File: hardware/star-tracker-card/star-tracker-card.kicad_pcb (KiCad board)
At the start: 4 copper layers, 99.8 x 94.6 mm, 329 parts, among them J1 ORESAT-DEBUG-CONNECTOR-CARD, J100 DM3BT-DSF-PEJS, J101 3-1734592-64-1734592-0, J102 FTSH-105-XX-X-DV-K, J3 CONN_03LONGPADS, J4 TFM-120-01-L-D-RA, Q1 MMBT2907, Q2 PMV45EN, Q3 DMP2240UDM, Q4 PMV45EN, Q5 MOSFET-PCH-SOT23-6, Q6 MOSFET-PCH-SOT23-6, U1 RCLAMP0504FB, U10 TLVH431, U11 TCAN330, U12 MIC842LYC5, U13 MIC842LYC5, U14 MAX4211FETE, U15 TPS62112, U16 MAX7310ATE, U17 25AAXX, U18 RCLAMP0504FB, U2 TPS2051CDBVR, U3 THGBMJG7C2LBAU8, U4 SN74LVC1G07DCK, U5 SN74LVC8T245MPWREPPW24-M, U6 CLVCH16T245MDGGREP, U7 OSD3358-512M-BSM, U8 TLV70028QDDCRQ1, U9 TCA9509DGKRDGK8-M, Y1 24MHz, Y2 ABS07-32.768KHZ-T

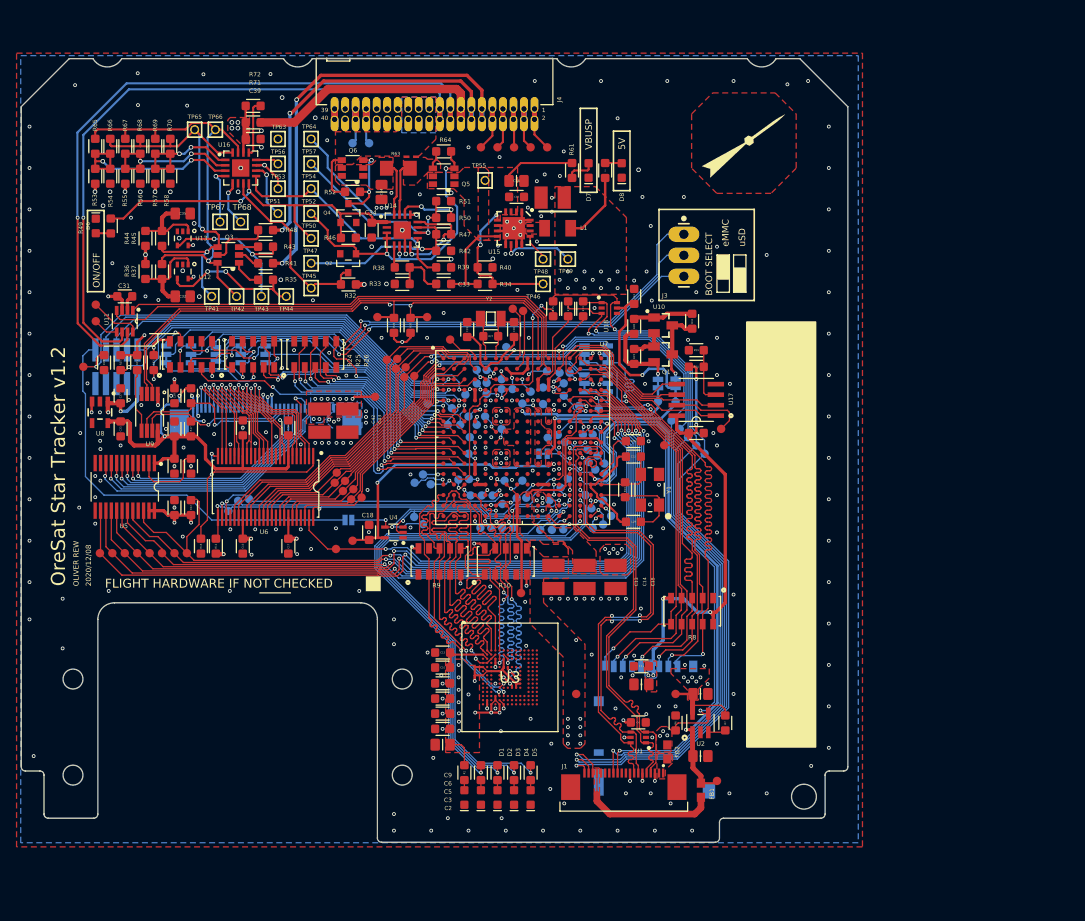
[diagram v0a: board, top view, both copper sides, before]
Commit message: More EAGLE import cleanup
Fixed sheets, did some ERC cleanup, imported into layout, impmorted 4 layer DRC rules.
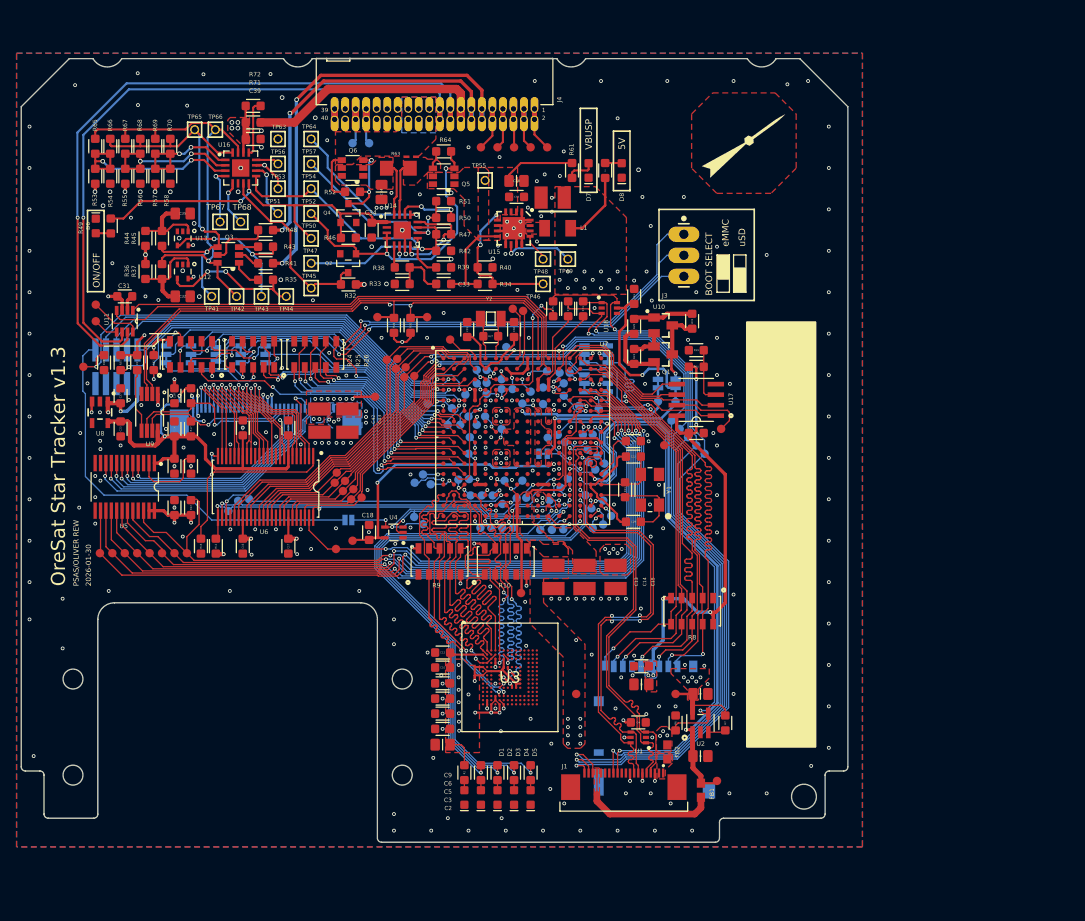
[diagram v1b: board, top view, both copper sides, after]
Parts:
- removed U$1: FLIGHMARKERNEW, star-tracker-card:FLIGHTMARKER_NEW_BOARDS
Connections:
- R35 pad 1: Net-(U12-OUT) -> Net-(R35-Pad1)
- R43 pad 1: Net-(U13-OUT) -> Net-(R43-Pad1)
- TP43 pad 1: Net-(U13-OUT) -> Net-(R43-Pad1)
- TP44 pad 1: Net-(U12-OUT) -> Net-(R35-Pad1)
- U12 pad 4: Net-(U12-OUT) -> unconnected-(U12-OUT-Pad4)
- U13 pad 4: Net-(U13-OUT) -> unconnected-(U13-OUT-Pad4)
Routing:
- net (no net): track 0.00 -> 36.0 mm, vias 0 -> 4
- net Net-(U13-OUT): track 19.0 -> 0.00 mm, vias 2 -> 0
- net Net-(U12-OUT): track 17.0 -> 0.00 mm, vias 2 -> 0
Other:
- board text added: "${ISSUE_DATE}"
- board text added: "OreSat Star Tracker v${REVISION}"
- board text added: "PSAS/OLIVER REW"
- board text removed: "2020/12/08"
- board text removed: "OLIVER REW"
- board text removed: "OreSat Star Tracker v1.2"

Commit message: Daily Push
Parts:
- removed C41: 0.1uF, star-tracker-card:.0603-A
- removed C44, C7: 10uF, star-tracker-card:.0805-B
- removed FB1: 30Ω/1.8A, star-tracker-card:0603
- removed J102: FTSH-105-XX-X-DV-K, star-tracker-card:CON10_2X5_DUK_FTSH
- removed JP1: JUMPER-SMT_2_NO_SILK, star-tracker-card:SMT-JUMPER_2_NO_SILK
- removed JP100: JUMPER-SMT_2_NC_TRACE_SILK, star-tracker-card:SMT-JUMPER_2_NC_TRACE_SILK
- removed R74, R75: 100, star-tracker-card:.0603-A
- removed TP112, TP151, TP155, TP58, TP59: TEST-POINT3X4, star-tracker-card:PAD.03X.04
- removed U18: RCLAMP0504FB, star-tracker-card:SC70-6
- added C45: 10u 25V 0805, Capacitor_SMD:C_1206_3216Metric, F.Cu at (222.8, 66.8)
- added C46: 470n, oresat-passives:c_0603-SMALL, F.Cu at (221.7, 73.8)
- added R76: 10k, oresat-passives:0603-C-NOSILK, F.Cu at (221.6, 75.9)
- added TP32: Test-Point, oresat-misc:TestPoint_Pad_D1.0mm, F.Cu at (221.1, 69.6)
- added TP71: TEST-POINT3X4, oresat-misc:TestPoint_Pad_D1.0mm, F.Cu at (216.8, 66.2)
- added TP72: TEST-POINT3X4, oresat-misc:TestPoint_Pad_D1.0mm, F.Cu at (216.8, 68.6)
- added TP73: TEST-POINT3X4, oresat-misc:TestPoint_Pad_D1.0mm, F.Cu at (216.8, 70.9)
- added TP74: TEST-POINT3X4, oresat-misc:TestPoint_Pad_D1.0mm, F.Cu at (212.5, 66.2)
- added TP75: TEST-POINT3X4, oresat-misc:TestPoint_Pad_D1.0mm, F.Cu at (212.5, 68.6)
- added TP76: TEST-POINT3X4, oresat-misc:TestPoint_Pad_D1.0mm, F.Cu at (212.5, 70.9)
- added TP77: TEST-POINT3X4, oresat-misc:TestPoint_Pad_D1.0mm, F.Cu at (212.5, 73.2)
- C1: value 10uF -> 100n; footprint star-tracker-card:.0805-B -> oresat-passives:c_0603-SMALL
- C10, C11, C12, C16, C17, C18, C19, C20, C21, C22, C23, C24, C25, C26, C27, C28, C29, C3, C30, C31, C33, C34, C37, C39, C4, C40, C5, C6, C9: footprint star-tracker-card:.0603-A -> oresat-passives:c_0603-SMALL
- C13, C14, C15, C36, C42, C43: footprint star-tracker-card:C1210 -> oresat-passives:0805-B-NOSILK
- C2, C38, C8: footprint star-tracker-card:.0805-B -> oresat-passives:0805-B-NOSILK
- C32, C35: footprint star-tracker-card:.0805-B-NOSILK -> oresat-passives:0805-C-NOSILK
- J1: footprint star-tracker-card:TE_2-1734592-0 -> oresat-connectors:J-JST-SM14BSHLSTF
- J4: footprint star-tracker-card:J-SAMTEC-TFM-120-X1-XXX-D-RA -> oresat-connectors:J-SAMTEC-TFM-120-X1-XXX-D-RA
- L1: footprint star-tracker-card:ECS-MPI4040 -> oresat-passives:L_ECS-MPI4040
- Q5, Q6: value MOSFET-PCH-SOT23-6 -> DMP3050LVT-7; footprint star-tracker-card:SOT23-6 -> Package_TO_SOT_SMD:TSOT-23-6
- R1, R11, R12, R13, R14, R15, R16, R17, R18, R19, R2, R20, R21, R22, R23, R27, R28, R29, R3, R30, R31, R32, R33, R34, R35, R36, R37, R38, R39, R4, R40, R41, R42, R43, R44, R45, R46, R47, R48, R49, R5, R50, R51, R52, R53, R54, R55, R56, R57, R58, R59, R6, R60, R61, R62, R64, R65, R66, R67, R68, R69, R70, R71, R72, R73: footprint star-tracker-card:.0603-A -> Resistor_SMD:R_0603_1608Metric
- R63: footprint star-tracker-card:R1206_334 -> Resistor_SMD:R_1206_3216Metric
- R7: value 10k -> 100; footprint star-tracker-card:.0603-A -> Resistor_SMD:R_0603_1608Metric
- TP1, TP10, TP100, TP101, TP102, TP103, TP104, TP105, TP106, TP107, TP108, TP109, TP11, TP110, TP111, TP113, TP114, TP115, TP116, TP117, TP118, TP119, TP12, TP120, TP121, TP122, TP123, TP124, TP125, TP126, TP127, TP128, TP129, TP13, TP130, TP131, TP132, TP133, TP134, TP135, TP136, TP137, TP138, TP139, TP14, TP140, TP141, TP142, TP143, TP144, TP145, TP146, TP147, TP148, TP149, TP15, TP150, TP152, TP153, TP154, TP156, TP157, TP158, TP159, TP16, TP160, TP161, TP162, TP163, TP164, TP165, TP166, TP167, TP168, TP169, TP17, TP170, TP171, TP172, TP173, TP174, TP175, TP176, TP177, TP178, TP179, TP18, TP180, TP181, TP182, TP183, TP184, TP19, TP2, TP20, TP21, TP22, TP23, TP24, TP25, TP26, TP27, TP28, TP29, TP3, TP30, TP31, TP35, TP36, TP37, TP38, TP39, TP4, TP40, TP5, TP6, TP60, TP61, TP62, TP69, TP7, TP8, TP9: footprint star-tracker-card:PAD.03X.04 -> oresat-misc:TestPoint_Pad_D1.0mm
- TP63: footprint star-tracker-card:2MM-TEST-POINT -> star-tracker-card:PAD.03X.04
- U12, U13: footprint star-tracker-card:SC70-5 -> Package_TO_SOT_SMD:SOT-353_SC-70-5
- U14, U16: footprint star-tracker-card:QFN65P400X400X80-17T210 -> Package_DFN_QFN:QFN-16-1EP_4x4mm_P0.65mm_EP2.1x2.1mm
- U15: footprint star-tracker-card:S-PVQFN-16 -> Package_DFN_QFN:Texas_RSA_VQFN-16-1EP_4x4mm_P0.65mm_EP2.7x2.7mm
- U2: value TPS2051CDBVR -> TS5A21366DCUR; footprint star-tracker-card:DBV5 -> Package_SO:VSSOP-8_2.3x2mm_P0.5mm
- U4: footprint star-tracker-card:C70(TI-DCK) -> Package_TO_SOT_SMD:SOT-353_SC-70-5
- moved TP65 13.6 mm to (107.1, 71.8)
- moved J1 12.3 mm to (174.9, 157.4), turned to 0 degrees
- moved TP66 11.7 mm to (111.8, 71.8)
- moved R54 9.26 mm to (104.5, 64.0), turned to 180 degrees
- moved R7 8.35 mm to (189.8, 143.6)
- moved R56 8.25 mm to (110.5, 64.0), turned to 180 degrees
- moved R58 7.86 mm to (116.5, 64.0), turned to 180 degrees
- moved R53 7.06 mm to (104.5, 65.5), turned to 180 degrees
- moved R57 6.57 mm to (116.5, 65.5), turned to 0 degrees
- moved R55 6.39 mm to (110.5, 65.5), turned to 0 degrees
- moved R69 6.29 mm to (119.5, 64.0), turned to 0 degrees
- moved R6 5.28 mm to (181.7, 141.3), turned to 180 degrees
- moved C1 5.27 mm to (177.7, 137.5), turned to -90 degrees
- moved R67 4.81 mm to (113.5, 64.0), turned to 180 degrees
- moved R65 4.23 mm to (107.5, 64.0), turned to 180 degrees
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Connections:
- net /star-tracker-card_2/BOOT0 renamed /Card Power Domain/BOOT0
- net /star-tracker-card_2/CB-RESET renamed /Card Power Domain/CB-RESET
- net /star-tracker-card_2/CB_CTRL renamed /Card Power Domain/CB_CTRL
- net /star-tracker-card_2/PB6/SCL renamed /Card Power Domain/PB6/SCL
- net /star-tracker-card_2/PB7/SDA renamed /Card Power Domain/PB7/SDA
- net /star-tracker-card_2/POUT renamed /Card Power Domain/POUT
- net /star-tracker-card_2/~{FAULT} renamed /Card Power Domain/~{FAULT}
- net /star-tracker-card_3/CLK_EN_E renamed /CLK_EN_E
- net /star-tracker-card_3/D0_E renamed /D0_E
- net /star-tracker-card_3/D10_E renamed /D10_E
- net /star-tracker-card_3/D11_E renamed /D11_E
- net /star-tracker-card_3/D1_E renamed /D1_E
- net /star-tracker-card_3/D2_E renamed /D2_E
- net /star-tracker-card_3/D3_E renamed /D3_E
- net /star-tracker-card_3/D4_E renamed /D4_E
- net /star-tracker-card_3/D5_E renamed /D5_E
- net /star-tracker-card_3/D6_E renamed /D6_E
- net /star-tracker-card_3/D7_E renamed /D7_E
- net /star-tracker-card_3/D8_E renamed /D8_E
- net /star-tracker-card_3/D9_E renamed /D9_E
- net /star-tracker-card_3/FLASH_E renamed /FLASH_E
- net /star-tracker-card_3/HSYNC_E renamed /HSYNC_E
- net /star-tracker-card_3/I2C2_SCL renamed /I2C2_SCL
- net /star-tracker-card_3/I2C2_SDA renamed /I2C2_SDA
- net /star-tracker-card_3/PIXCLK_E renamed /PIXCLK_E
- net /star-tracker-card_3/SADDR_E renamed /SADDR_E
- net /star-tracker-card_3/STANDBY_E renamed /STANDBY_E
- net /star-tracker-card_3/TRIGGER_E renamed /TRIGGER_E
- net /star-tracker-card_3/VREG_EN_E renamed /VREG_EN_E
- net /star-tracker-card_3/VSYNC_E renamed /VSYNC_E
- net /star-tracker-card_3/~{OE_E} renamed /~{OE_E}
- net /star-tracker-card_3/~{RESET_E} renamed /~{RESET_E}
- net /star-tracker-card_4/OSC0_GND renamed /SIP B/OSC0_GND
- net /star-tracker-card_4/OSC0_IN renamed /SIP B/OSC0_IN
- net /star-tracker-card_4/OSC0_OUT renamed /SIP B/OSC0_OUT
- net CAN2_H renamed /CAN2_H
- net CAN2_L renamed /CAN2_L
- net OPD_PWR renamed /OPD_PWR
- net OPD_SCL renamed /OPD_SCL
- net OPD_SDA renamed /OPD_SDA
- net USB_CLI_VBUS renamed /V_USB
- C1 pad 1: /star-tracker-card_4/VOUT_USB -> /Card Power Domain/ON/~{OFF}
- C13 pad 1: VIN_USB -> /SIP A, E ,F/VIN_USB
- C34 pad 1: /star-tracker-card_2/ON/~{OFF} -> /Card Power Domain/ON/~{OFF}
- C4 pad 1: VIN_USB -> /SIP A, E ,F/VIN_USB
- D1 pad A: Net-(D1-PadA) -> (no net)
- D1 pad C: GND -> (no net)
- D2 pad A: Net-(D2-PadA) -> (no net)
- D2 pad C: GND -> (no net)
- D3 pad A: Net-(D3-PadA) -> (no net)
- D3 pad C: GND -> (no net)
- D4 pad A: Net-(D4-PadA) -> (no net)
- D4 pad C: GND -> (no net)
- D5 pad A: Net-(D5-PadA) -> (no net)
- D5 pad C: GND -> (no net)
- D6 pad A: Net-(D6-PadA) -> (no net)
- D6 pad C: GND -> (no net)
- D7 pad A: Net-(D7-PadA) -> (no net)
- D7 pad C: GND -> (no net)
- D8 pad A: Net-(D8-PadA) -> (no net)
- D8 pad C: GND -> (no net)
- FB2 pad 2: VIN_USB -> /SIP A, E ,F/VIN_USB
- J1 pad 12: UART0_RX -> unconnected-(J1-SWCLK-Pad12)
- J1 pad 13: UART0_TX -> unconnected-(J1-SWO-Pad13)
- J1 pad 14: unconnected-(J1-SWDIO-Pad14) -> GND
- J1 pad 15: unconnected-(J1-SWCLK-Pad15) -> GND
- J1 pad 16: unconnected-(J1-SWO-Pad16) -> GND
- J1 pad 3: GND -> /USB_CLI_P
- J1 pad 4: USB_CLI_P -> /USB_CLI_N
- J1 pad 5: USB_CLI_N -> GND
- J1 pad 6: GND -> /UART0_TX
- J1 pad 7: USB_HO_PX -> /UART0_RX
- J1 pad 8: USB_HO_N -> Net-(J1-DEBUG-0)
- J1 pad 9: GND -> unconnected-(J1-VTARGET-Pad9)
- J4 pad 1: /star-tracker-card_1/N$103 -> Net-(J4-Pad1)
- J4 pad 10: /star-tracker-card_1/SPARE1 -> unconnected-(J4-Pad10)
- J4 pad 2: /star-tracker-card_1/N$103 -> Net-(J4-Pad1)
- J4 pad 21: VBUS -> unconnected-(J4-Pad21)
- J4 pad 22: VBUS -> unconnected-(J4-Pad22)
- J4 pad 3: /star-tracker-card_1/SPARE4 -> Net-(J4-Pad3)
- J4 pad 31: GND -> unconnected-(J4-Pad31)
- J4 pad 32: GND -> Net-(J4-Pad32)
- J4 pad 33: /star-tracker-card_1/CAN1_H -> Net-(J4-Pad32)
- J4 pad 34: /star-tracker-card_1/CAN1_H -> Net-(J4-Pad34)
- J4 pad 35: /star-tracker-card_1/CAN1_L -> Net-(J4-Pad34)
- J4 pad 36: /star-tracker-card_1/CAN1_L -> unconnected-(J4-Pad36)
- J4 pad 37: GND -> /C3-UART-TX
- J4 pad 38: GND -> /C3-UART-RX
- J4 pad 39: /star-tracker-card_1/~{SD} -> unconnected-(J4-Pad39)
- J4 pad 4: /star-tracker-card_1/SPARE4 -> Net-(J4-Pad3)
- J4 pad 40: /star-tracker-card_1/~{SD} -> unconnected-(J4-Pad40)
- J4 pad 5: /star-tracker-card_1/SPARE3 -> Net-(J4-Pad5)
- J4 pad 6: /star-tracker-card_1/SPARE3 -> Net-(J4-Pad5)
- J4 pad 7: /star-tracker-card_1/SPARE2 -> unconnected-(J4-Pad7)
- J4 pad 8: /star-tracker-card_1/SPARE2 -> unconnected-(J4-Pad8)
- J4 pad 9: /star-tracker-card_1/SPARE1 -> unconnected-(J4-Pad9)
- JP101 pad 1: Net-(TP165-1) -> Net-(U7A-SYS_VDD3_3P3V@1)
- JP102 pad 1: /star-tracker-card_3/D0_I -> /Camera Logical Level Shifters/D0_I
- JP103 pad 1: /star-tracker-card_3/D1_I -> /Camera Logical Level Shifters/D1_I
- JP110 pad 1: /star-tracker-card_3/D2_I -> /Camera Logical Level Shifters/D2_I
- JP111 pad 1: /star-tracker-card_3/D3_I -> /SIP C/D3_I
- Q3 pad 2: Net-(Q3B-S) -> /Card Power Domain/PEN-SDA-FILT
- Q3 pad 4: /star-tracker-card_2/PEN-SDA-FILT -> Net-(Q3B-D)
- Q3 pad 5: Net-(Q3A-S) -> /Card Power Domain/PEN-SCL-FILT
- Q3 pad 6: /star-tracker-card_2/PEN-SCL-FILT -> Net-(Q3A-D)
- Q4 pad 1: /star-tracker-card_2/ON/~{OFF} -> /Card Power Domain/ON/~{OFF}
- Q5 pad 1: VBUSP -> Net-(U14-RS-)
- Q5 pad 2: VBUSP -> Net-(U14-RS-)
- Q5 pad 4: Net-(Q5-S) -> VBUSP
- Q5 pad 5: VBUSP -> Net-(U14-RS-)
- Q5 pad 6: VBUSP -> Net-(U14-RS-)
- Q6 pad 1: Net-(U14-RS+) -> VBUS
- Q6 pad 2: Net-(U14-RS+) -> VBUS
- Q6 pad 4: VBUS -> Net-(Q6-S)
- Q6 pad 5: Net-(U14-RS+) -> VBUS
- Q6 pad 6: Net-(U14-RS+) -> VBUS
- R1 pad 2: Net-(D1-PadA) -> Net-(D1-A)
- R11 pad 1: /star-tracker-card_3/BUS_OE -> /Camera Logical Level Shifters/BUS_OE
- R12 pad 1: /star-tracker-card_3/INPUT_EN -> /Camera Logical Level Shifters/INPUT_EN
- R19 pad 2: Net-(TP31-1) -> Net-(U7B-TRSTN)
- R2 pad 2: Net-(D2-PadA) -> Net-(D2-A)
- R29 pad 2: /star-tracker-card_3/SDA_2 -> /Camera Logical Level Shifters/SDA_2
- R3 pad 2: Net-(D3-PadA) -> Net-(D3-A)
- R30 pad 2: /star-tracker-card_3/SCL_2 -> /Camera Logical Level Shifters/SCL_2
- R35 pad 1: Net-(R35-Pad1) -> Net-(U12-OUT)
- R37 pad 2: /star-tracker-card_2/PEN-SCL-FILT -> /Card Power Domain/PEN-SCL-FILT
- R4 pad 2: Net-(D4-PadA) -> Net-(D4-A)
- R41 pad 2: Net-(Q3B-S) -> Net-(Q3B-D)
- R43 pad 1: Net-(R43-Pad1) -> Net-(U13-OUT)
- R45 pad 2: /star-tracker-card_2/PEN-SDA-FILT -> /Card Power Domain/PEN-SDA-FILT
- R46 pad 2: /star-tracker-card_2/ON/~{OFF} -> /Card Power Domain/ON/~{OFF}
- R48 pad 2: Net-(Q3A-S) -> Net-(Q3A-D)
- R49 pad 1: Net-(D6-PadA) -> Net-(D6-A)
- R49 pad 2: /star-tracker-card_2/ON/~{OFF} -> /Card Power Domain/ON/~{OFF}
- R5 pad 2: Net-(D5-PadA) -> Net-(D5-A)
- R53 pad 1: /star-tracker-card_2/AD2 -> /Card Power Domain/AD2
- R54 pad 1: GND -> /Card Power Domain/AD2
- R54 pad 2: /star-tracker-card_2/AD2 -> GND
- R55 pad 1: /star-tracker-card_2/AD1 -> VPD
- R55 pad 2: VPD -> /Card Power Domain/AD1
- R56 pad 1: GND -> /Card Power Domain/AD1
- R56 pad 2: /star-tracker-card_2/AD1 -> GND
- R57 pad 1: /star-tracker-card_2/AD0 -> VPD
- R57 pad 2: VPD -> /Card Power Domain/AD0
- R58 pad 1: GND -> /Card Power Domain/AD0
- R58 pad 2: /star-tracker-card_2/AD0 -> GND
- R6 pad 2: Net-(U2-EN) -> Net-(U16-IO7)
- R61 pad 1: Net-(D7-PadA) -> Net-(D7-A)
- R62 pad 1: Net-(D8-PadA) -> Net-(D8-A)
- R63 pad 1: Net-(U14-RS+) -> Net-(Q6-S)
- R63 pad 2: Net-(Q5-S) -> Net-(U14-RS-)
- R64 pad 2: Net-(Q5-S) -> Net-(U14-RS-)
- R65 pad 1: /star-tracker-card_2/PEN-SCL-FILT -> /Card Power Domain/PEN-SCL-FILT
- R65 pad 2: /star-tracker-card_2/AD2 -> /Card Power Domain/AD2
- R66 pad 1: /star-tracker-card_2/AD2 -> /Card Power Domain/PEN-SDA-FILT
- R66 pad 2: /star-tracker-card_2/PEN-SDA-FILT -> /Card Power Domain/AD2
- R67 pad 1: /star-tracker-card_2/PEN-SCL-FILT -> /Card Power Domain/PEN-SCL-FILT
- R67 pad 2: /star-tracker-card_2/AD1 -> /Card Power Domain/AD1
- R68 pad 1: /star-tracker-card_2/AD1 -> /Card Power Domain/PEN-SDA-FILT
- R68 pad 2: /star-tracker-card_2/PEN-SDA-FILT -> /Card Power Domain/AD1
- R69 pad 1: /star-tracker-card_2/PEN-SCL-FILT -> /Card Power Domain/AD0
- R69 pad 2: /star-tracker-card_2/AD0 -> /Card Power Domain/PEN-SCL-FILT
- R7 pad 1: Net-(U2-~{FLT}) -> /C3-UART-RX
- R7 pad 2: VDD -> Net-(U2-NO1)
- R70 pad 1: /star-tracker-card_2/AD0 -> /Card Power Domain/PEN-SDA-FILT
- R70 pad 2: /star-tracker-card_2/PEN-SDA-FILT -> /Card Power Domain/AD0
- R73 pad 1: I2C0_SCL -> /C3-UART-TX
- R73 pad 2: Net-(U7A-I2C0_SCL) -> Net-(U2-NO2)
- TP41 pad 1: /star-tracker-card_2/PEN-SDA-FILT -> /Card Power Domain/PEN-SDA-FILT
- TP42 pad 1: /star-tracker-card_2/PEN-SCL-FILT -> /Card Power Domain/PEN-SCL-FILT
- TP43 pad 1: Net-(R43-Pad1) -> Net-(U13-OUT)
- TP44 pad 1: Net-(R35-Pad1) -> Net-(U12-OUT)
- TP50 pad 1: /star-tracker-card_2/ON/~{OFF} -> /Card Power Domain/ON/~{OFF}
- TP65 pad 1: /star-tracker-card_2/PEN-SDA-FILT -> /Card Power Domain/PEN-SDA-FILT
- TP66 pad 1: /star-tracker-card_2/PEN-SCL-FILT -> /Card Power Domain/PEN-SCL-FILT
- U1 pad 1: USB_CLI_N -> /USB_CLI_N
- U1 pad 3: USB_CLI_P -> /USB_CLI_P
- U1 pad 4: USB_HO_PX -> unconnected-(U1-I3-Pad4)
- U1 pad 5: VIN_USB -> /SIP A, E ,F/VIN_USB
- U1 pad 6: USB_HO_N -> unconnected-(U1-I4-Pad6)
- U11 pad 5: Net-(TP35-1) -> Net-(U11-SHDN)
- U11 pad 8: Net-(TP40-1) -> Net-(U11-S)
- U12 pad 3: (no net) -> unconnected-(U12-Pad3)
- U12 pad 4: unconnected-(U12-OUT-Pad4) -> Net-(U12-OUT)
- U13 pad 3: (no net) -> unconnected-(U13-Pad3)
- U13 pad 4: unconnected-(U13-OUT-Pad4) -> Net-(U13-OUT)
- U14 pad 1: /star-tracker-card_2/ON/~{OFF} -> /Card Power Domain/ON/~{OFF}
- U14 pad 15: Net-(Q5-S) -> Net-(U14-RS-)
- U14 pad 16: Net-(U14-RS+) -> Net-(Q6-S)
- U14 pad 2: (no net) -> /Card Power Domain/ON/~{OFF}
- U16 pad 1: /star-tracker-card_2/AD0 -> /Card Power Domain/AD0
- U16 pad 15: /star-tracker-card_2/PEN-SCL-FILT -> /Card Power Domain/PEN-SCL-FILT
- U16 pad 16: /star-tracker-card_2/PEN-SDA-FILT -> /Card Power Domain/PEN-SDA-FILT
- U16 pad 2: /star-tracker-card_2/AD1 -> /Card Power Domain/AD1
- U16 pad 3: /star-tracker-card_2/AD2 -> /Card Power Domain/AD2
- U16 pad 8: /star-tracker-card_2/ON/~{OFF} -> /Card Power Domain/ON/~{OFF}
- U17 pad 7: Net-(TP69-1) -> Net-(U17-~{HOLD})
- U2 pad 1: /star-tracker-card_4/VOUT_USB -> Net-(U2-NO1)
- U2 pad 2: GND -> /UART0_TX
- U2 pad 3: Net-(U2-~{FLT}) -> Net-(U16-IO7)
- U2 pad 4: Net-(U2-EN) -> GND
- U2 pad 5: VDD -> Net-(U2-NO2)
- U4 pad 1: (no net) -> unconnected-(U4-Pad1)
- U4 pad 2: /star-tracker-card_5/PMIC_PGOOD -> /SIP A, E ,F/PMIC_PGOOD
- U4 pad 4: RESET# -> Net-(U4-Y)
- U5 pad 14: /star-tracker-card_3/VREG_EN -> /Camera Logical Level Shifters/VREG_EN
- U5 pad 15: /star-tracker-card_3/TRIGGER -> /Camera Logical Level Shifters/TRIGGER
- U5 pad 16: /star-tracker-card_3/SADDR -> /Camera Logical Level Shifters/SADDR
- U5 pad 17: /star-tracker-card_3/CAM_OE -> /Camera Logical Level Shifters/CAM_OE
- U5 pad 18: /star-tracker-card_3/STANDBY -> /Camera Logical Level Shifters/STANDBY
- U5 pad 19: /star-tracker-card_3/RESET -> /Camera Logical Level Shifters/RESET
- U5 pad 20: /star-tracker-card_3/CLK_EN -> /Camera Logical Level Shifters/CLK_EN
- U5 pad 22: /star-tracker-card_3/INPUT_EN -> /Camera Logical Level Shifters/INPUT_EN
- U6 pad 25: /star-tracker-card_3/BUS_OE -> /Camera Logical Level Shifters/BUS_OE
- U6 pad 26: /star-tracker-card_3/VSYNC_I -> /Camera Logical Level Shifters/VSYNCI
- U6 pad 27: /star-tracker-card_3/HSYNC_I -> /Camera Logical Level Shifters/HSYNC_I
- U6 pad 29: /star-tracker-card_3/PIXCLK_I -> /Camera Logical Level Shifters/PIXCLK_I
- U6 pad 30: /star-tracker-card_3/D6_I -> /Camera Logical Level Shifters/D6_I
- U6 pad 32: /star-tracker-card_3/D5_I -> /Camera Logical Level Shifters/D5_I
- U6 pad 33: /star-tracker-card_3/D4_I -> /Camera Logical Level Shifters/D4_I
- U6 pad 35: /star-tracker-card_3/D3_I -> /SIP C/D3_I
- U6 pad 36: /star-tracker-card_3/D2_I -> /Camera Logical Level Shifters/D2_I
- U6 pad 37: /star-tracker-card_3/D1_I -> /Camera Logical Level Shifters/D1_I
- U6 pad 38: /star-tracker-card_3/D0_I -> /Camera Logical Level Shifters/D0_I
- U6 pad 40: /star-tracker-card_3/D7_I -> /Camera Logical Level Shifters/D7_I
- U6 pad 41: /star-tracker-card_3/D8_I -> /Camera Logical Level Shifters/D8_I
- U6 pad 43: /star-tracker-card_3/D9_I -> /Camera Logical Level Shifters/D9_I
- U6 pad 44: /star-tracker-card_3/D10_I -> /Camera Logical Level Shifters/D10_I
- U6 pad 46: /star-tracker-card_3/D11_I -> /Camera Logical Level Shifters/D11_I
- U6 pad 47: /star-tracker-card_3/FLASH -> /Camera Logical Level Shifters/FLASH
- U6 pad 48: /star-tracker-card_3/BUS_OE -> /Camera Logical Level Shifters/BUS_OE
- U7 pad A1: /star-tracker-card_3/D4_I -> /Camera Logical Level Shifters/D4_I
- U7 pad A10: /star-tracker-card_3/SCL_2 -> /Camera Logical Level Shifters/SCL_2
- U7 pad A12: UART0_RX -> /UART0_RX
- U7 pad A2: /star-tracker-card_3/D5_I -> /Camera Logical Level Shifters/D5_I
- U7 pad A3: /star-tracker-card_3/D8_I -> /Camera Logical Level Shifters/D8_I
- U7 pad A4: Net-(TP30-1) -> Net-(U7C-XDMA_EVENT_INTR0)
- U7 pad A7: Net-(TP182-1) -> Net-(U7B-SYS_ADC_1P8V)
- U7 pad A8: Net-(TP39-1) -> Net-(U7B-AIN0)
- U7 pad A9: Net-(TP171-1) -> Net-(U7B-AGND_ADC)
- U7 pad B1: /star-tracker-card_3/D7_I -> /Camera Logical Level Shifters/D7_I
- U7 pad B10: /star-tracker-card_3/SDA_2 -> /Camera Logical Level Shifters/SDA_2
- U7 pad B12: UART0_TX -> /UART0_TX
- U7 pad B2: /star-tracker-card_3/D6_I -> /Camera Logical Level Shifters/D6_I
- U7 pad B3: /star-tracker-card_3/D9_I -> /Camera Logical Level Shifters/D9_I
- U7 pad B4: /star-tracker-card_3/PIXCLK_I -> /Camera Logical Level Shifters/PIXCLK_I
- U7 pad B6: Net-(TP181-1) -> Net-(U7B-AIN2)
- U7 pad B7: Net-(TP171-1) -> Net-(U7B-AGND_ADC)
- U7 pad B8: Net-(TP38-1) -> Net-(U7B-AIN1)
- U7 pad B9: Net-(TP171-1) -> Net-(U7B-AGND_ADC)
- U7 pad C1: Net-(J102-NC/TDI) -> unconnected-(U7B-TDI-PadC1)
- U7 pad C12: Net-(TP177-1) -> Net-(U7C-UART0_CTSN)
- U7 pad C13: Net-(TP178-1) -> Net-(U7C-UART0_RTSN)
- U7 pad C2: Net-(J102-SWO/TDO) -> unconnected-(U7B-TDO-PadC2)
- U7 pad C3: /star-tracker-card_3/D10_I -> /Camera Logical Level Shifters/D10_I
- U7 pad C4: /star-tracker-card_3/D11_I -> /Camera Logical Level Shifters/D11_I
- U7 pad C5: Net-(TP180-1) -> Net-(U7C-ECAP0_IN_PWM0_OUT)
- U7 pad C6: Net-(TP175-1) -> Net-(U7B-AIN3)
- U7 pad C7: Net-(TP176-1) -> Net-(U7B-AIN4)
- U7 pad C8: Net-(TP169-1) -> Net-(U7B-AIN5)
- U7 pad C9: Net-(TP179-1) -> Net-(U7B-AIN6)
- U7 pad D1: Net-(J102-SWDCLK/TCK) -> unconnected-(U7B-TCK-PadD1)
- U7 pad D12: Net-(TP172-1) -> Net-(U7F-NC@1)
- U7 pad D13: Net-(TP174-1) -> Net-(U7D-MDC)
- U7 pad D14: /star-tracker-card_3/STANDBY -> /Camera Logical Level Shifters/STANDBY
- U7 pad D15: /star-tracker-card_3/SADDR -> /Camera Logical Level Shifters/SADDR
- U7 pad D16: /star-tracker-card_3/RESET -> /Camera Logical Level Shifters/RESET
- U7 pad D2: Net-(J102-SWDIO/TMS) -> unconnected-(U7B-TMS-PadD2)
- U7 pad D3: Net-(TP31-1) -> Net-(U7B-TRSTN)
- U7 pad D4: Net-(TP167-1) -> Net-(U7A-EXTINTN)
- U7 pad D5: Net-(TP173-1) -> Net-(U7F-CAP_VDD_RTC)
- U7 pad D6: Net-(TP168-1) -> Net-(U7B-PMIC_MUX_OUT)
- U7 pad D7: Net-(TP170-1) -> Net-(U7B-AIN7)
- U7 pad E1: Net-(TP159-1) -> Net-(U7D-LCD_AC_BIAS_EN)
- U7 pad E13: Net-(TP158-1) -> Net-(U7D-MDIO)
- U7 pad E14: /star-tracker-card_3/INPUT_EN -> /Camera Logical Level Shifters/INPUT_EN
- U7 pad E15: /star-tracker-card_3/TRIGGER -> /Camera Logical Level Shifters/TRIGGER
- U7 pad E16: /star-tracker-card_3/CLK_EN -> /Camera Logical Level Shifters/CLK_EN
- U7 pad E4: Net-(TP167-1) -> Net-(U7A-EXTINTN)
- U7 pad F1: Net-(TP162-1) -> Net-(U7D-LCD_PCLK)
- U7 pad F10: Net-(TP163-1) -> Net-(U7A-SYS_VDD_1P8V@1)
- U7 pad F11: Net-(TP161-1) -> Net-(U7A-SYS_VDD2_3P3V@1)
- U7 pad F13: Net-(TP160-1) -> Net-(U7F-VDD_MPU)
- U7 pad F14: /star-tracker-card_3/BUS_OE -> /Camera Logical Level Shifters/BUS_OE
- U7 pad F15: /star-tracker-card_3/CAM_OE -> /Camera Logical Level Shifters/CAM_OE
- U7 pad F16: /star-tracker-card_3/VREG_EN -> /Camera Logical Level Shifters/VREG_EN
- U7 pad F2: Net-(TP152-1) -> Net-(U7D-LCD_HSYNC)
- U7 pad F3: Net-(TP153-1) -> Net-(U7D-LCD_VSYNC)
- U7 pad F4: Net-(TP156-1) -> Net-(U7F-VDDS_DDR)
- U7 pad F8: Net-(TP165-1) -> Net-(U7A-SYS_VDD3_3P3V@1)
- U7 pad F9: Net-(TP165-1) -> Net-(U7A-SYS_VDD3_3P3V@1)
- U7 pad G10: Net-(TP163-1) -> Net-(U7A-SYS_VDD_1P8V@1)
- U7 pad G11: Net-(TP161-1) -> Net-(U7A-SYS_VDD2_3P3V@1)
- U7 pad G13: Net-(TP166-1) -> Net-(U7F-VDDS_PLL)
- U7 pad G14: Net-(TP148-1) -> Net-(U7D-MII1_TX_EN)
- U7 pad G15: /star-tracker-card_3/FLASH -> /Camera Logical Level Shifters/FLASH
- U7 pad G16: Net-(TP135-1) -> Net-(U7D-MII1_TXD2)
- U7 pad G4: Net-(TP154-1) -> Net-(U7F-VDD_CORE)
- U7 pad G8: Net-(TP165-1) -> Net-(U7A-SYS_VDD3_3P3V@1)
- U7 pad G9: Net-(TP165-1) -> Net-(U7A-SYS_VDD3_3P3V@1)
- U7 pad H10: Net-(TP163-1) -> Net-(U7A-SYS_VDD_1P8V@1)
- U7 pad H11: Net-(TP163-1) -> Net-(U7A-SYS_VDD_1P8V@1)
- U7 pad H14: Net-(TP149-1) -> Net-(U7D-MII1_TXD1)
- U7 pad H15: Net-(TP137-1) -> Net-(U7D-MII1_TXD0)
- U7 pad H16: Net-(TP147-1) -> Net-(U7D-MII1_TX_CLK)
- U7 pad H6: Net-(TP157-1) -> Net-(U7F-VPP)
- U7 pad H7: Net-(TP165-1) -> Net-(U7A-SYS_VDD3_3P3V@1)
- U7 pad H8: Net-(TP165-1) -> Net-(U7A-SYS_VDD3_3P3V@1)
- U7 pad H9: Net-(TP165-1) -> Net-(U7A-SYS_VDD3_3P3V@1)
- U7 pad J10: Net-(TP163-1) -> Net-(U7A-SYS_VDD_1P8V@1)
- U7 pad J11: Net-(TP163-1) -> Net-(U7A-SYS_VDD_1P8V@1)
- U7 pad J14: Net-(TP143-1) -> Net-(U7D-RMII1_REF_CLK)
- U7 pad J15: Net-(TP139-1) -> Net-(U7B-USB0_DRVVBUS)
- U7 pad J16: VIN_USB -> /SIP A, E ,F/VIN_USB
- U7 pad J6: Net-(TP150-1) -> Net-(U7F-NC@2)
- U7 pad J7: Net-(TP165-1) -> Net-(U7A-SYS_VDD3_3P3V@1)
- U7 pad J8: Net-(TP165-1) -> Net-(U7A-SYS_VDD3_3P3V@1)
- U7 pad J9: Net-(TP165-1) -> Net-(U7A-SYS_VDD3_3P3V@1)
- U7 pad K10: Net-(TP163-1) -> Net-(U7A-SYS_VDD_1P8V@1)
- U7 pad K13: Net-(TP141-1) -> Net-(U7B-USB0_CE)
- U7 pad K14: Net-(TP138-1) -> Net-(U7B-USB0_ID)
- U7 pad K15: USB_CLI_P -> /USB_CLI_P
- U7 pad K16: USB_CLI_N -> /USB_CLI_N
- U7 pad K4: Net-(TP145-1) -> Net-(U7F-NC@3)
- U7 pad K8: Net-(TP165-1) -> Net-(U7A-SYS_VDD3_3P3V@1)
- U7 pad K9: Net-(TP165-1) -> Net-(U7A-SYS_VDD3_3P3V@1)
- U7 pad L10: Net-(TP163-1) -> Net-(U7A-SYS_VDD_1P8V@1)
- U7 pad L13: Net-(TP144-1) -> Net-(U7B-USB1_CE)
- U7 pad L15: USB_HO_PX -> Net-(U7B-USB1_DP)
- U7 pad L16: USB_HO_N -> Net-(U7B-USB1_DM)
- U7 pad L4: Net-(TP140-1) -> Net-(U7A-EXT_WAKEUP)
- U7 pad L8: Net-(TP165-1) -> Net-(U7A-SYS_VDD3_3P3V@1)
- U7 pad L9: Net-(TP165-1) -> Net-(U7A-SYS_VDD3_3P3V@1)
- U7 pad M1: Net-(TP134-1) -> Net-(U7C-GPMC_ADVN_ALE)
- U7 pad M13: Net-(TP136-1) -> Net-(U7A-PMIC_NRESET)
- U7 pad M14: Net-(U2-EN) -> Net-(U7B-USB1_DRVVBUS)
- U7 pad M15: /star-tracker-card_4/VOUT_USB -> Net-(U7B-USB1_VBUS)
- U7 pad M4: Net-(TP140-1) -> Net-(U7A-EXT_WAKEUP)
- U7 pad N1: Net-(TP128-1) -> Net-(U7C-GPMC_OEN_REN)
- U7 pad N10: Net-(TP121-1) -> Net-(U7A-PMIC_POWER_EN)
- U7 pad N11: Net-(TP121-1) -> Net-(U7A-PMIC_POWER_EN)
- U7 pad N12: /star-tracker-card_5/PMIC_PGOOD -> /SIP A, E ,F/PMIC_PGOOD
- U7 pad N13: Net-(TP133-1) -> Net-(U7B-PMIC_MUX_IN)
- U7 pad N14: Net-(TP125-1) -> Net-(U7C-GPMC_BEN1)
- U7 pad N2: Net-(TP127-1) -> Net-(U7C-GPMC_WEN)
- U7 pad N3: Net-(TP131-1) -> Net-(U7C-GPMC_BEN0_CLE)
- U7 pad N4: Net-(TP132-1) -> Net-(U7A-PMIC_LDO_PGOOD)
- U7 pad N5: Net-(TP132-1) -> Net-(U7A-PMIC_LDO_PGOOD)
- U7 pad N6: Net-(TP129-1) -> Net-(U7A-PMIC_TS)
- U7 pad N7: Net-(TP130-1) -> Net-(U7A-PMIC_BAT_SENSE)
- U7 pad P11: /star-tracker-card_5/PMIC_PGOOD -> /SIP A, E ,F/PMIC_PGOOD
- U7 pad P12: Net-(TP126-1) -> Net-(U7C-GPMC_A2)
- U7 pad P15: Net-(TP114-1) -> Net-(U7C-GPMC_WAIT0)
- U7 pad P3: Net-(TP122-1) -> Net-(U7C-GPMC_CSN0)
- U7 pad P5: Net-(TP123-1) -> Net-(U7C-GPMC_AD9)
- U7 pad P6: Net-(TP124-1) -> Net-(U7C-GPMC_AD12)
- U7 pad P7: /star-tracker-card_3/HSYNC_I -> /Camera Logical Level Shifters/HSYNC_I
- U7 pad P8: Net-(TP130-1) -> Net-(U7A-PMIC_BAT_SENSE)
- U7 pad P9: VIN_USB -> /SIP A, E ,F/VIN_USB
- U7 pad R11: RESET# -> Net-(U4-Y)
- U7 pad R12: Net-(TP118-1) -> Net-(U7C-GPMC_A1)
- U7 pad R15: Net-(TP117-1) -> Net-(U7C-GPMC_A10)
- U7 pad R16: Net-(TP111-1) -> Net-(U7C-GPMC_WPN)
- U7 pad R5: Net-(TP115-1) -> Net-(U7C-GPMC_AD10)
- U7 pad R6: Net-(TP120-1) -> Net-(U7C-GPMC_AD13)
- U7 pad R7: Net-(TP107-1) -> Net-(U7C-GPMC_CSN3)
- U7 pad R8: Net-(TP130-1) -> Net-(U7A-PMIC_BAT_SENSE)
- U7 pad R9: VIN_USB -> /SIP A, E ,F/VIN_USB
- U7 pad T11: Net-(TP102-1) -> Net-(U7A-PMIC_PB_IN)
- U7 pad T12: Net-(TP100-1) -> Net-(U7C-GPMC_A0)
- U7 pad T13: Net-(TP101-1) -> Net-(U7C-GPMC_A3)
- U7 pad T15: Net-(TP108-1) -> Net-(U7C-GPMC_A9)
- U7 pad T16: Net-(TP103-1) -> Net-(U7C-GPMC_A11)
- U7 pad T4: Net-(TP104-1) -> Net-(U7C-GPMC_AD8)
- U7 pad T5: Net-(TP105-1) -> Net-(U7C-GPMC_AD11)
- U7 pad T6: /star-tracker-card_3/VSYNC_I -> /Camera Logical Level Shifters/VSYNCI
- U7 pad T7: Net-(TP106-1) -> Net-(U7C-GPMC_CLK)
- U7 pad T8: Net-(TP130-1) -> Net-(U7A-PMIC_BAT_SENSE)
- U7 pad T9: VIN_USB -> /SIP A, E ,F/VIN_USB
- U9 pad 2: /star-tracker-card_3/SCL_2 -> /Camera Logical Level Shifters/SCL_2
- U9 pad 3: /star-tracker-card_3/SDA_2 -> /Camera Logical Level Shifters/SDA_2
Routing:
- net /star-tracker-card_3/INPUT_EN: track 94.9 -> 0.00 mm, vias 2 -> 0
- net /Camera Logical Level Shifters/INPUT_EN: track 0.00 -> 94.9 mm, vias 0 -> 2
- net /star-tracker-card_3/TRIGGER: track 94.5 -> 0.00 mm, vias 2 -> 0
- net /Camera Logical Level Shifters/TRIGGER: track 0.00 -> 94.5 mm, vias 0 -> 2
- net /star-tracker-card_3/SADDR: track 94.4 -> 0.00 mm, vias 2 -> 0
- net /Camera Logical Level Shifters/SADDR: track 0.00 -> 94.4 mm, vias 0 -> 2
- net /star-tracker-card_3/VREG_EN: track 93.0 -> 0.00 mm, vias 2 -> 0
- net /Camera Logical Level Shifters/VREG_EN: track 0.00 -> 93.0 mm, vias 0 -> 2
- net /star-tracker-card_3/STANDBY: track 92.8 -> 0.00 mm, vias 2 -> 0
- net /Camera Logical Level Shifters/STANDBY: track 0.00 -> 92.8 mm, vias 0 -> 2
- net /star-tracker-card_3/RESET: track 90.8 -> 0.00 mm, vias 2 -> 0
- net /Camera Logical Level Shifters/RESET: track 0.00 -> 90.8 mm, vias 0 -> 2
- net I2C0_SCL: track 89.7 -> 0.00 mm, vias 2 -> 0
- net /C3-UART-TX: track 0.00 -> 89.7 mm, vias 0 -> 2
- net /star-tracker-card_3/CAM_OE: track 89.6 -> 0.00 mm, vias 2 -> 0
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- added copper zone on F.Cu, net /SIP A, E ,F/VIN_USB
- added copper zone on In2.Cu, net /SIP A, E ,F/VIN_USB
- added copper zone on F.Cu, net Net-(Q6-S)
- added copper zone on F.Cu, net Net-(U14-RS-)
- added copper zone on F.Cu, net Net-(U7A-SYS_VDD2_3P3V@1)
- added copper zone on F.Cu, net Net-(U7A-SYS_VDD3_3P3V@1)
- added copper zone on F.Cu, net Net-(U7A-SYS_VDD_1P8V@1)
- removed copper zone on F.Cu, net Net-(Q5-S)
- removed copper zone on F.Cu, net Net-(TP161-1)
- removed copper zone on F.Cu, net Net-(TP163-1)
- removed copper zone on F.Cu, net Net-(TP165-1)
- removed copper zone on F.Cu, net Net-(U14-RS+)
- removed copper zone on F.Cu, net USB_HO_VBUS
- removed copper zone on F.Cu, net VIN_USB
- removed copper zone on In2.Cu, net VIN_USB
